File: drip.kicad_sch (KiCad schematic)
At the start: 43 parts, among them Q1 2n2222, Q2 2n2222, Q3 2n2222, Q4 2n2222, Q5 2n2222, Q6 2n2222, Q7 2n2222, Q8 2n2222, SW1 8, SW10 Divide, SW11 Divide, SW12 Divide, SW2 5, SW3 2, SW4 Decimal, SW5 9, SW6 6, SW7 3, SW8 CHS, SW9 Divide, U1 SA39-12YWA, U2 SA39-12YWA, U3 SA39-12YWA, U4 SA39-12YWA, U5 SA39-12YWA, U6 SA39-12YWA, U7 SA39-12YWA, U8 SA39-12YWA

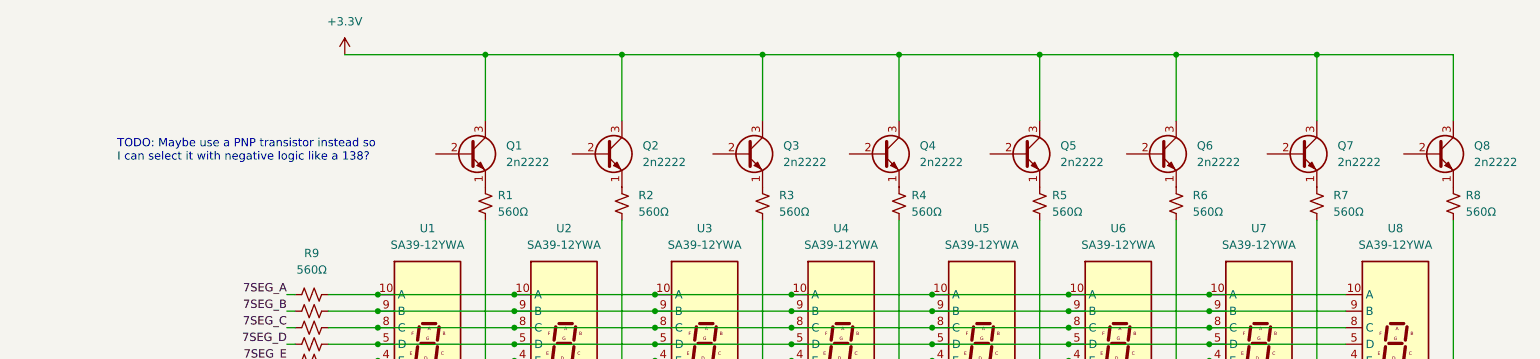
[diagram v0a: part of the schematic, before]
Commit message: PNP transistors to prepare for '138 based
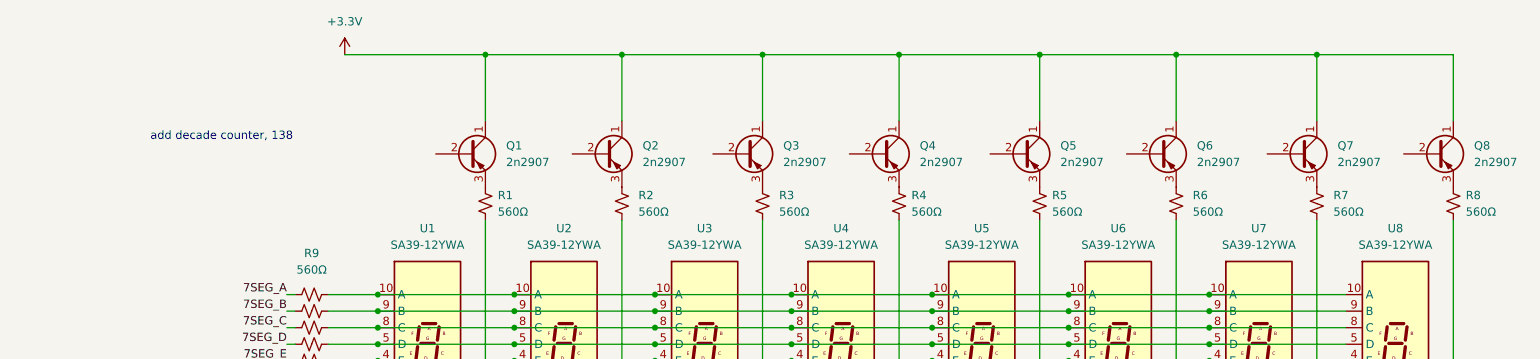
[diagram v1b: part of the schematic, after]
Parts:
- removed Q1, Q2, Q3, Q4, Q5, Q6, Q7, Q8: 2n2222, Package_TO_SOT_THT:TO-92_Inline, symbol Device:Q_NPN_EBC
- added Q1, Q2, Q3, Q4, Q5, Q6, Q7, Q8: 2n2907, Package_TO_SOT_THT:TO-92_Inline, symbol Device:Q_PNP_CBE
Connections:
- net +3V3: now also Q1.1 (C), Q2.1 (C), Q3.1 (C), Q4.1 (C), Q5.1 (C), Q6.1 (C), Q7.1 (C), Q8.1 (C)
- net at R4.2: now also Q4.3 (E)
- net at R7.2: now also Q7.3 (E)
- net at R6.2: now also Q6.3 (E)
- net at R2.2: now also Q2.3 (E)
- net at R3.2: now also Q3.3 (E)
- net at R1.2: now also Q1.3 (E)
- net at R5.2: now also Q5.3 (E)
- net at R8.2: now also Q8.3 (E)
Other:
- note added: "add decade counter, 138"
- note removed: "TODO: Maybe use a PNP transistor instead so I can select it with negative logic like a 138?"

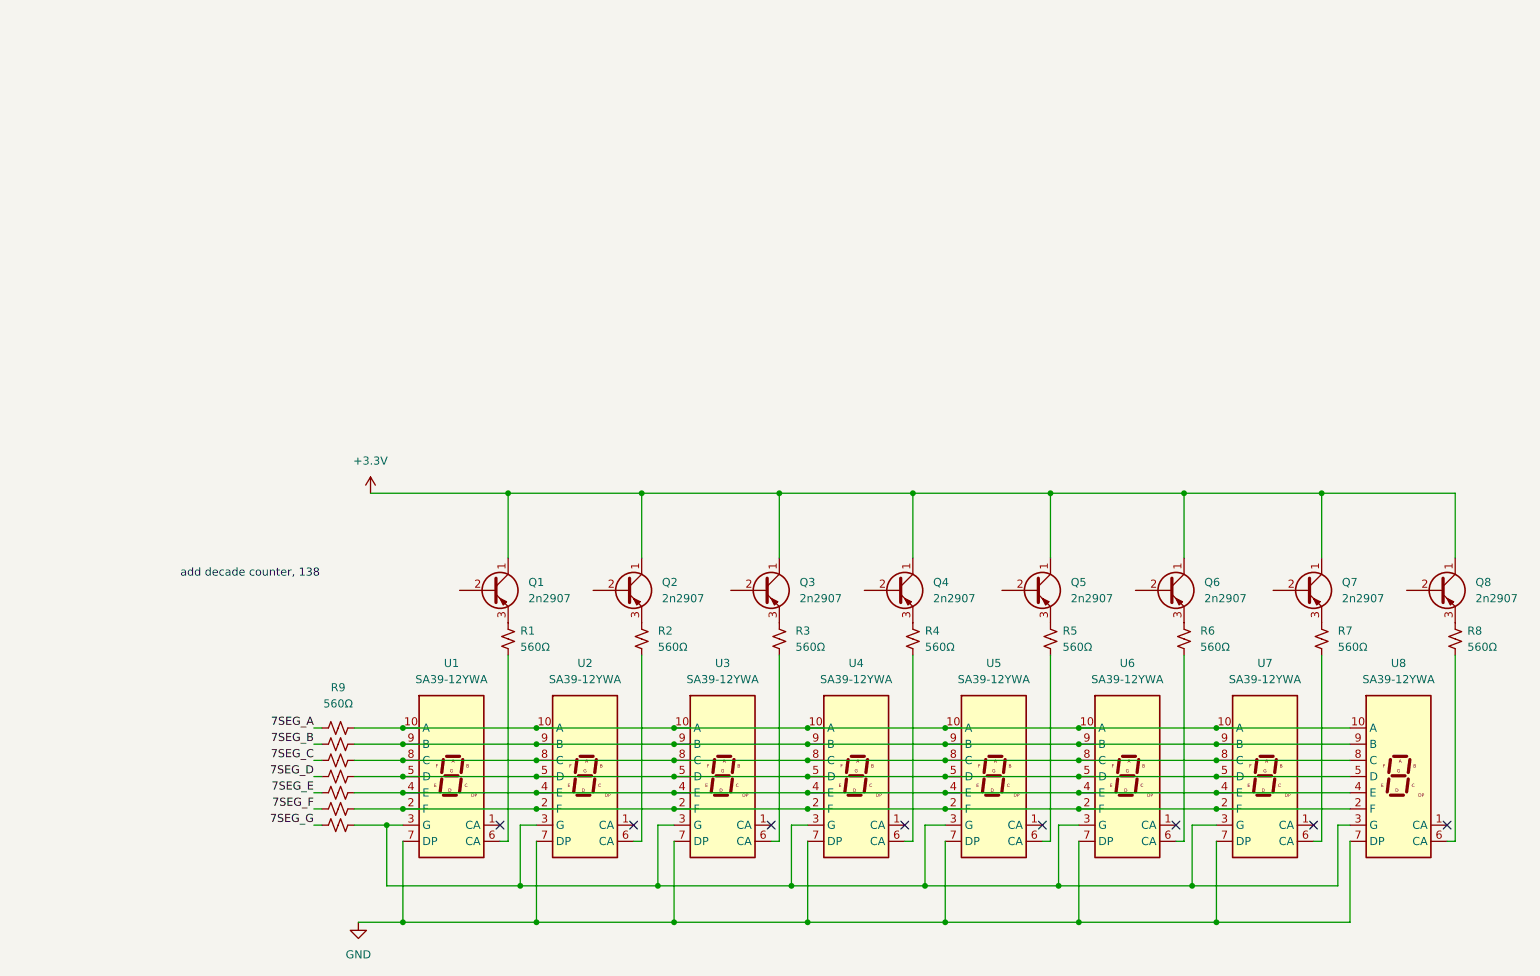
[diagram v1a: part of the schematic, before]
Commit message: Untested first draft at 5641AS 7-seg 4-digit LED
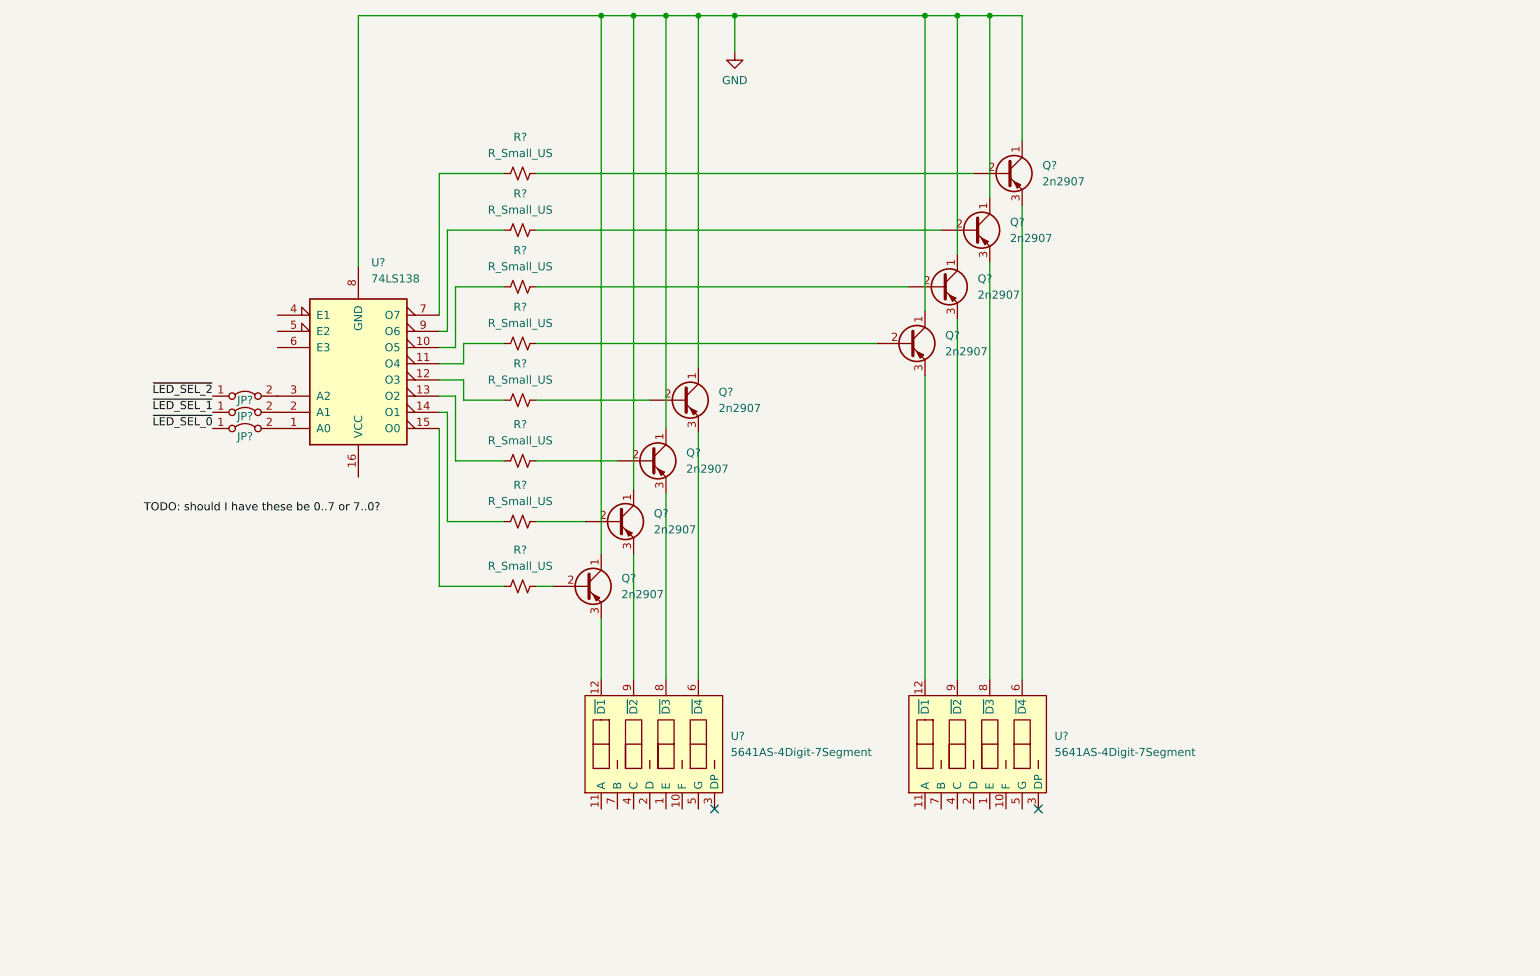
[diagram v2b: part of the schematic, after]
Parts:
- removed Q1, Q2, Q3, Q4, Q5, Q6, Q7, Q8: 2n2907, Package_TO_SOT_THT:TO-92_Inline, symbol Device:Q_PNP_CBE
- removed R1, R10, R11, R12, R13, R14, R15, R2, R3, R4, R5, R6, R7, R8, R9: 560Ω, Resistor_THT:R_Axial_DIN0204_L3.6mm_D1.6mm_P5.08mm_Horizontal, symbol Device:R_Small_US
- removed U1, U2, U3, U4, U5, U6, U7, U8: SA39-12YWA, Display_7Segment:Sx39-1xxxxx, symbol Display_Character:SA39-12YWA
- added JP? (x3): Jumper_2_Bridged, Jumper:SolderJumper-2_P1.3mm_Bridged2Bar_RoundedPad1.0x1.5mm, symbol Jumper:Jumper_2_Bridged
- added Q? (x8): 2n2907, Package_TO_SOT_THT:TO-92_Inline, symbol Device:Q_PNP_CBE
- added R? (x8): R_Small_US, symbol Device:R_Small_US
- added U? (x2): 5641AS-4Digit-7Segment, 5641AS:5641AS_THT, symbol 5641AS:5641AS-4Digit-7Segment
- added U?: 74LS138, symbol 74xx:74LS138
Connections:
- net GND: now also Q?.1 (C), Q?.1 (C), Q?.1 (C), Q?.1 (C), Q?.1 (C), Q?.1 (C), Q?.1 (C), Q?.1 (C), U?.8 (GND)
- new net: Q?.2 (B), R?.2 (x8)
- new net: Q?.3 (E), U?.6 (~{D4}) (x2)
- new net: Q?.3 (E), U?.12 (~{D1}) (x2)
- new net: Q?.3 (E), U?.8 (~{D3}) (x2)
- new net: Q?.3 (E), U?.9 (~{D2}) (x2)
- new net: R?.1, U?.13 (O2)
- new net: R?.1, U?.7 (O7)
- new net: JP?.2 (B), U?.1 (A0)
- new net: R?.1, U?.10 (O5)
- new net: R?.1, U?.11 (O4)
- new net: R?.1, U?.12 (O3)
- new net: R?.1, U?.14 (O1)
- new net: R?.1, U?.15 (O0)
- new net: JP?.2 (B), U?.2 (A1)
- new net: JP?.2 (B), U?.3 (A2)
- new net: R?.1, U?.9 (O6)
- new net ~{LED_SEL_0}: JP?.1 (A)
- new net ~{LED_SEL_1}: JP?.1 (A)
- new net ~{LED_SEL_2}: JP?.1 (A)
- no-connect marks 8 -> 2
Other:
- note removed: "add decade counter, 138"

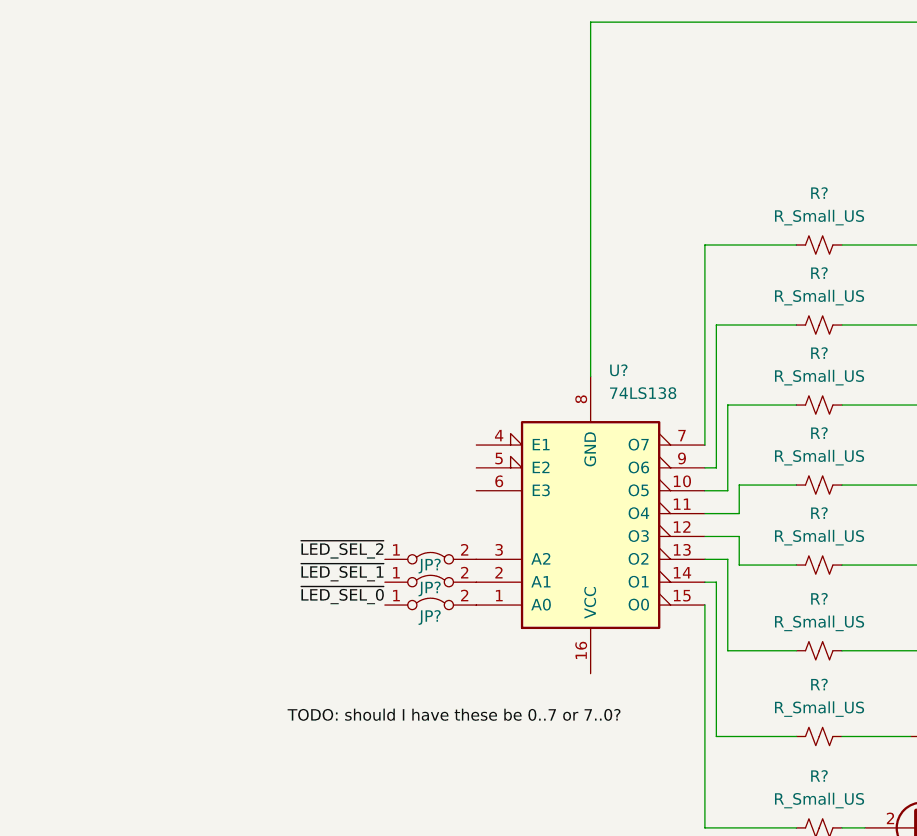
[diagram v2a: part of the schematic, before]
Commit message: '138 wired up
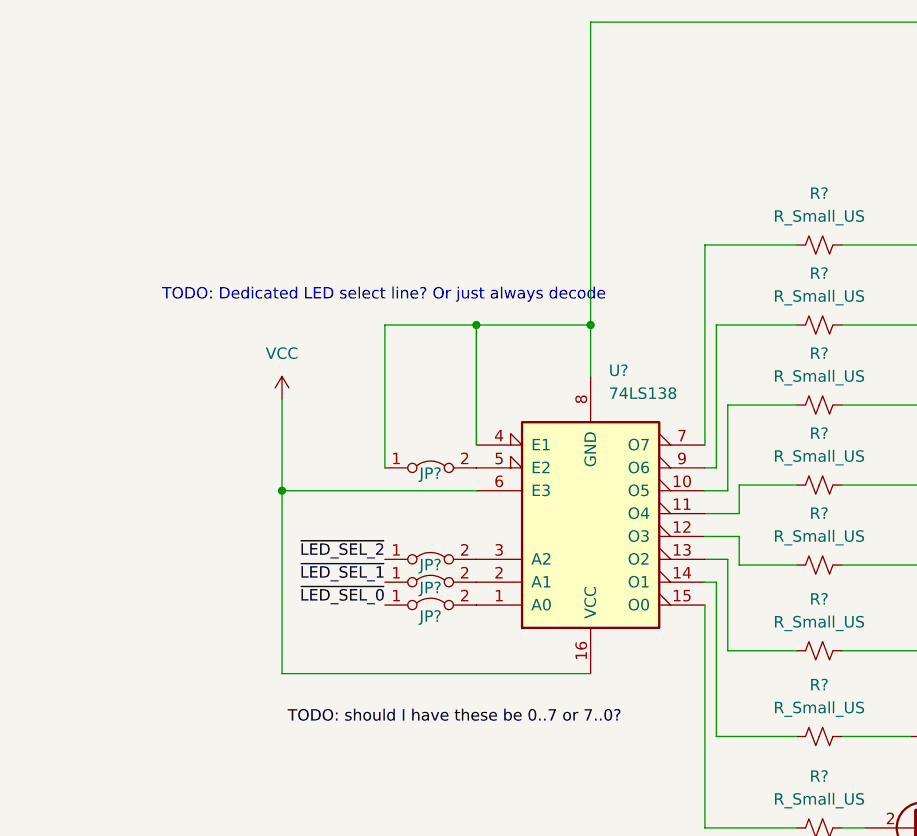
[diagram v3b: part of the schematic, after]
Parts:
- added JP?: Jumper_2_Bridged, Jumper:SolderJumper-2_P1.3mm_Bridged2Bar_RoundedPad1.0x1.5mm, symbol Jumper:Jumper_2_Bridged
- U?: footprint (none) -> Package_DIP:DIP-16_W7.62mm_Socket_LongPads
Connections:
- net GND: now also U?.4 (E1), JP?.1 (A)
- net VCC: now reaches U?.16 (VCC)
- net VCC: now also U?.6 (E3)
- net at U?.5 (E2): now also JP?.2 (B)
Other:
- note added: "TODO: Dedicated LED select line? Or just always decode"
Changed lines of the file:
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@@
 (kicad_sch (version 20211123) (generator eeschema)
   (paper "A2")
+  (junction (at 347.98 235.585) (diameter 0) (color 0 0 0 0)
+  )
   (junction (at 408.94 201.93) (diameter 0) (color 0 0 0 0)
   )
@@
   (junction (at 398.78 201.93) (diameter 0) (color 0 0 0 0)
   )
+  (junction (at 360.68 235.585) (diameter 0) (color 0 0 0 0)
+  )
   (junction (at 414.02 201.93) (diameter 0) (color 0 0 0 0)
+  )
+  (junction (at 326.39 254) (diameter 0) (color 0 0 0 0)
   )
   (no_connect (at 467.36 326.39))
@@
     (stroke (width 0) (type default) (color 0 0 0 0))
   )
+  (wire (pts (xy 337.82 251.46) (xy 337.82 235.585))
+    (stroke (width 0) (type default) (color 0 0 0 0))
+  )
   (wire (pts (xy 408.94 201.93) (xy 414.02 201.93))
     (stroke (width 0) (type default) (color 0 0 0 0))
   )
+  (wire (pts (xy 347.98 248.92) (xy 347.98 235.585))
+    (stroke (width 0) (type default) (color 0 0 0 0))
+  )
   (wire (pts (xy 377.19 259.08) (xy 373.38 259.08))
     (stroke (width 0) (type default) (color 0 0 0 0))
@@
     (stroke (width 0) (type default) (color 0 0 0 0))
   )
+  (wire (pts (xy 337.82 235.585) (xy 347.98 235.585))
+    (stroke (width 0) (type default) (color 0 0 0 0))
+  )
   (wire (pts (xy 377.19 253.365) (xy 383.54 253.365))
     (stroke (width 0) (type default) (color 0 0 0 0))
@@
     (stroke (width 0) (type default) (color 0 0 0 0))
   )
-  (wire (pts (xy 360.68 241.3) (xy 360.68 201.93))
+  (wire (pts (xy 360.68 241.3) (xy 360.68 235.585))
     (stroke (width 0) (type default) (color 0 0 0 0))
   )
@@
     (stroke (width 0) (type default) (color 0 0 0 0))
   )
+  (wire (pts (xy 360.68 274.32) (xy 326.39 274.32))
+    (stroke (width 0) (type default) (color 0 0 0 0))
+  )
+  (wire (pts (xy 360.68 235.585) (xy 360.68 201.93))
+    (stroke (width 0) (type default) (color 0 0 0 0))
+  )
   (wire (pts (xy 449.58 258.445) (xy 449.58 306.07))
     (stroke (width 0) (type default) (color 0 0 0 0))
@@
     (stroke (width 0) (type default) (color 0 0 0 0))
   )
+  (wire (pts (xy 326.39 254) (xy 347.98 254))
+    (stroke (width 0) (type default) (color 0 0 0 0))
+  )
   (wire (pts (xy 414.02 267.335) (xy 414.02 306.07))
     (stroke (width 0) (type default) (color 0 0 0 0))
@@
     (stroke (width 0) (type default) (color 0 0 0 0))
   )
+  (wire (pts (xy 326.39 274.32) (xy 326.39 254))
+    (stroke (width 0) (type default) (color 0 0 0 0))
+  )
   (wire (pts (xy 454.66 201.93) (xy 449.58 201.93))
     (stroke (width 0) (type default) (color 0 0 0 0))
@@
     (stroke (width 0) (type default) (color 0 0 0 0))
   )
+  (wire (pts (xy 347.98 235.585) (xy 360.68 235.585))
+    (stroke (width 0) (type default) (color 0 0 0 0))
+  )
   (wire (pts (xy 398.78 286.385) (xy 398.78 201.93))
     (stroke (width 0) (type default) (color 0 0 0 0))
@@
     (stroke (width 0) (type default) (color 0 0 0 0))
   )
+  (wire (pts (xy 326.39 243.84) (xy 326.39 254))
+    (stroke (width 0) (type default) (color 0 0 0 0))
+  )
   (wire (pts (xy 459.74 201.93) (xy 459.74 230.505))
     (stroke (width 0) (type default) (color 0 0 0 0))
@@
   (wire (pts (xy 464.82 221.615) (xy 464.82 201.93))
     (stroke (width 0) (type default) (color 0 0 0 0))
+  )
+  (text "TODO: Dedicated LED select line? Or just always decode"
+    (at 313.055 233.045 0)
+    (effects (font (size 1.27 1.27)) (justify left bottom))
   )
   (label "~{LED_SEL_1}" (at 337.82 264.16 180)
@@
       (effects (font (size 1.27 1.27)) (justify left))
     )
-    (property "Footprint" "" (id 2) (at 360.68 259.08 0)
+    (property "Footprint" "Package_DIP:DIP-16_W7.62mm_Socket_LongPads" (id 2) (at 360.68 259.08 0)
       (effects (font (size 1.27 1.27)) hide)
     )
@@
     (pin "1")
   )
+  (symbol (lib_id "power:VCC") (at 326.39 243.84 0) (unit 1)
+    (in_bom yes) (on_board yes) (fields_autoplaced)
+    (property "Reference" "#PWR?" (id 0) (at 326.39 247.65 0)
+      (effects (font (size 1.27 1.27)) hide)
+    )
+    (property "Value" "VCC" (id 1) (at 326.39 238.76 0))
+    (property "Footprint" "" (id 2) (at 326.39 243.84 0)
+      (effects (font (size 1.27 1.27)) hide)
+    )
+    (property "Datasheet" "" (id 3) (at 326.39 243.84 0)
+      (effects (font (size 1.27 1.27)) hide)
+    )
+    (pin "1")
+  )
   (symbol (lib_id "Device:Q_PNP_CBE") (at 411.48 262.255 0) (unit 1)
     (in_bom yes) (on_board yes) (fields_autoplaced)
@@
     (pin "2")
   )
+  (symbol (lib_id "Jumper:Jumper_2_Bridged") (at 342.9 251.46 0) (unit 1)
+    (in_bom no) (on_board yes)
+    (property "Reference" "JP?" (id 0) (at 342.9 252.095 0))
+    (property "Value" "Jumper_2_Bridged" (id 1) (at 342.9 247.65 0)
+      (effects (font (size 1.27 1.27)) hide)
+    )
+    (property "Footprint" "Jumper:SolderJumper-2_P1.3mm_Bridged2Bar_RoundedPad1.0x1.5mm" (id 2) (at 342.9 251.46 0)
+      (effects (font (size 1.27 1.27)) hide)
+    )
+    (property "Datasheet" "~" (id 3) (at 342.9 251.46 0)
+      (effects (font (size 1.27 1.27)) hide)
+    )
+    (pin "1")
+    (pin "2")
+  )
   (symbol (lib_id "Switch:SW_Push_45deg") (at 153.67 320.675 0) (unit 1)
     (in_bom yes) (on_board yes) (fields_autoplaced)
@@
       (reference "#PWR?") (unit 1) (value "GND") (footprint "")
     )
+    (path "/367b19f6-9d6d-4f1c-bcc8-5f64ffbc1e8e"
+      (reference "#PWR?") (unit 1) (value "VCC") (footprint "")
+    )
     (path "/2dde6d7a-b96e-4b5e-a160-a4e51b2f8210"
       (reference "JP?") (unit 1) (value "Jumper_2_Bridged") (footprint "Jumper:SolderJumper-2_P1.3mm_Bridged2Bar_RoundedPad1.0x1.5mm")
     )
+    (path "/8b7a5ff1-bfc4-473f-a51a-f734693c1551"
+      (reference "JP?") (unit 1) (value "Jumper_2_Bridged") (footprint "Jumper:SolderJumper-2_P1.3mm_Bridged2Bar_RoundedPad1.0x1.5mm")
+    )
     (path "/bd177a76-74ef-41bd-b539-cbc5b870b9f8"
       (reference "JP?") (unit 1) (value "Jumper_2_Bridged") (footprint "Jumper:SolderJumper-2_P1.3mm_Bridged2Bar_RoundedPad1.0x1.5mm")
@@
     )
     (path "/1c7d349c-d2da-4ef6-a8a5-45ed3856b2b6"
-      (reference "U?") (unit 1) (value "74LS138") (footprint "")
+      (reference "U?") (unit 1) (value "74LS138") (footprint "Package_DIP:DIP-16_W7.62mm_Socket_LongPads")
     )
     (path "/6705b112-b4f7-49f5-bf15-d8c399a84605"

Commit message: LED driver done
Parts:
- added J1: ISP, Connector_PinHeader_2.54mm:PinHeader_1x04_P2.54mm_Vertical, symbol Connector:Conn_01x04_Male
- added U4: MSP430G2553IN20, Package_DIP:DIP-20_W7.62mm, symbol MCU_Texas_MSP430:MSP430G2553IN20
- gave numbers to parts that had none: 23
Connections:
- net GND: now also J1.4 (Pin_4), U4.20 (DVSS)
- net VCC: now also J1.1 (Pin_1), U4.1 (DVCC)
- net d4: now reaches U3.1 (E)
- net d4: now also U2.1 (E), U4.6 (TCK/SMCLK/UCB0STE/UCA0CLK/VREF+/VeREF+/CA4/A4/P1.4)
- net d5: now reaches U3.10 (F)
- net d5: now also U2.10 (F), U4.7 (TMS/UCB0CLK/UCA0STE/TA0.0/CA5/A5/P1.5)
- net d0: now reaches U3.11 (A)
- net d0: now also U2.11 (A), U4.2 (TA0CLK/ACLK/CA0/A0/P1.0)
- net d3: now reaches U3.2 (D)
- net d3: now also U2.2 (D), U4.5 (CAOUT/VREF-/VeREF-/CA3/A3/P1.3)
- net d7: now reaches U3.3 (DP)
- net d7: now also U2.3 (DP), U4.15 (TDO/TDI/UCB0SIMO/UCB0SDA/CAOUT/CA7/A7/P1.7)
- net d2: now reaches U3.4 (C)
- net d2: now also U2.4 (C), U4.4 (UCA0TXD/UCA0SIMO/TA0.1/CA2/A2/P1.2)
- net d6: now reaches U3.5 (G)
- net d6: now also U2.5 (G), U4.14 (TDI/TCLK/UCB0SOMI/UCB0SCL/TA0.1/CA6/A6/P1.6)
- net d1: now reaches U3.7 (B)
- net d1: now also U2.7 (B), U4.3 (UCA0RXD/UCA0SOMI/TA0.0/CA1/A1/P1.1)
- new net TEST: J1.2 (Pin_2), U4.17 (TEST/SBWTCK)
- new net ~{RST}: J1.3 (Pin_3), U4.16 (~{RST}/NMI/SBWTDIO)
- no-connect marks 2 -> 0
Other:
- note added: "TODO: Can I run a 74ls138 on 3.3v?"
- note added: "TODO: Do I really need an 8-bit data?"
- note added: "TODO: Does 0..7 make more sense than 7..0?"
